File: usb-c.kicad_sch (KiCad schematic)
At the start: 37 parts, among them J2 USB-C_GCT_USB4105-GF-A, U12 FUSB303B, U13 AP22615B_TSOT26

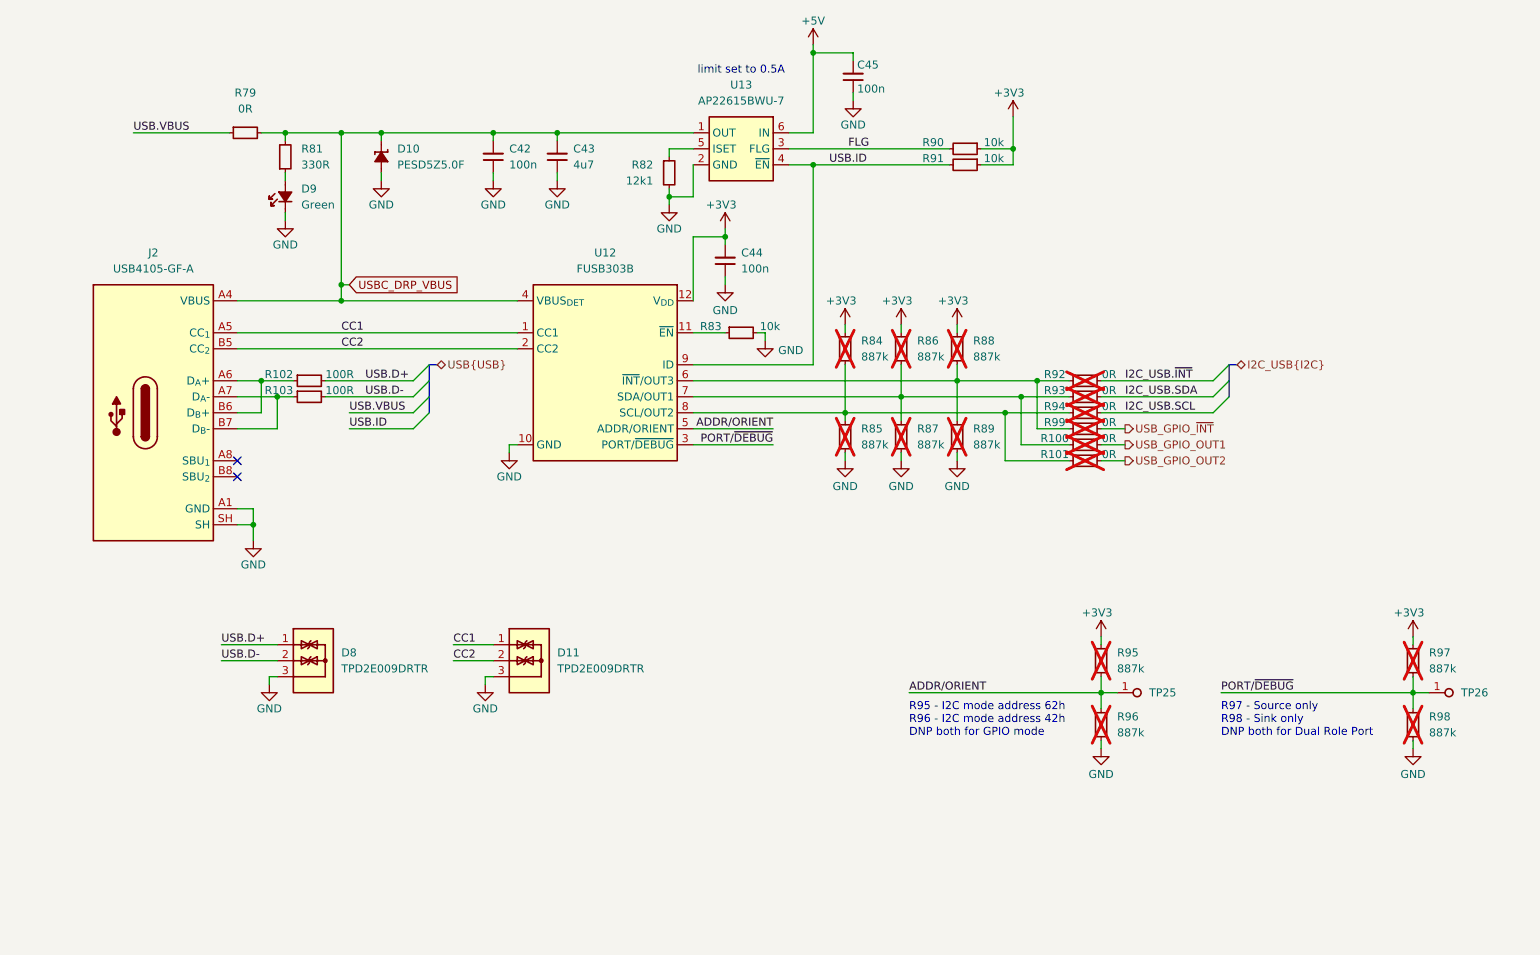
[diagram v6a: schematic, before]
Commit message: [#95036] Add testpoints
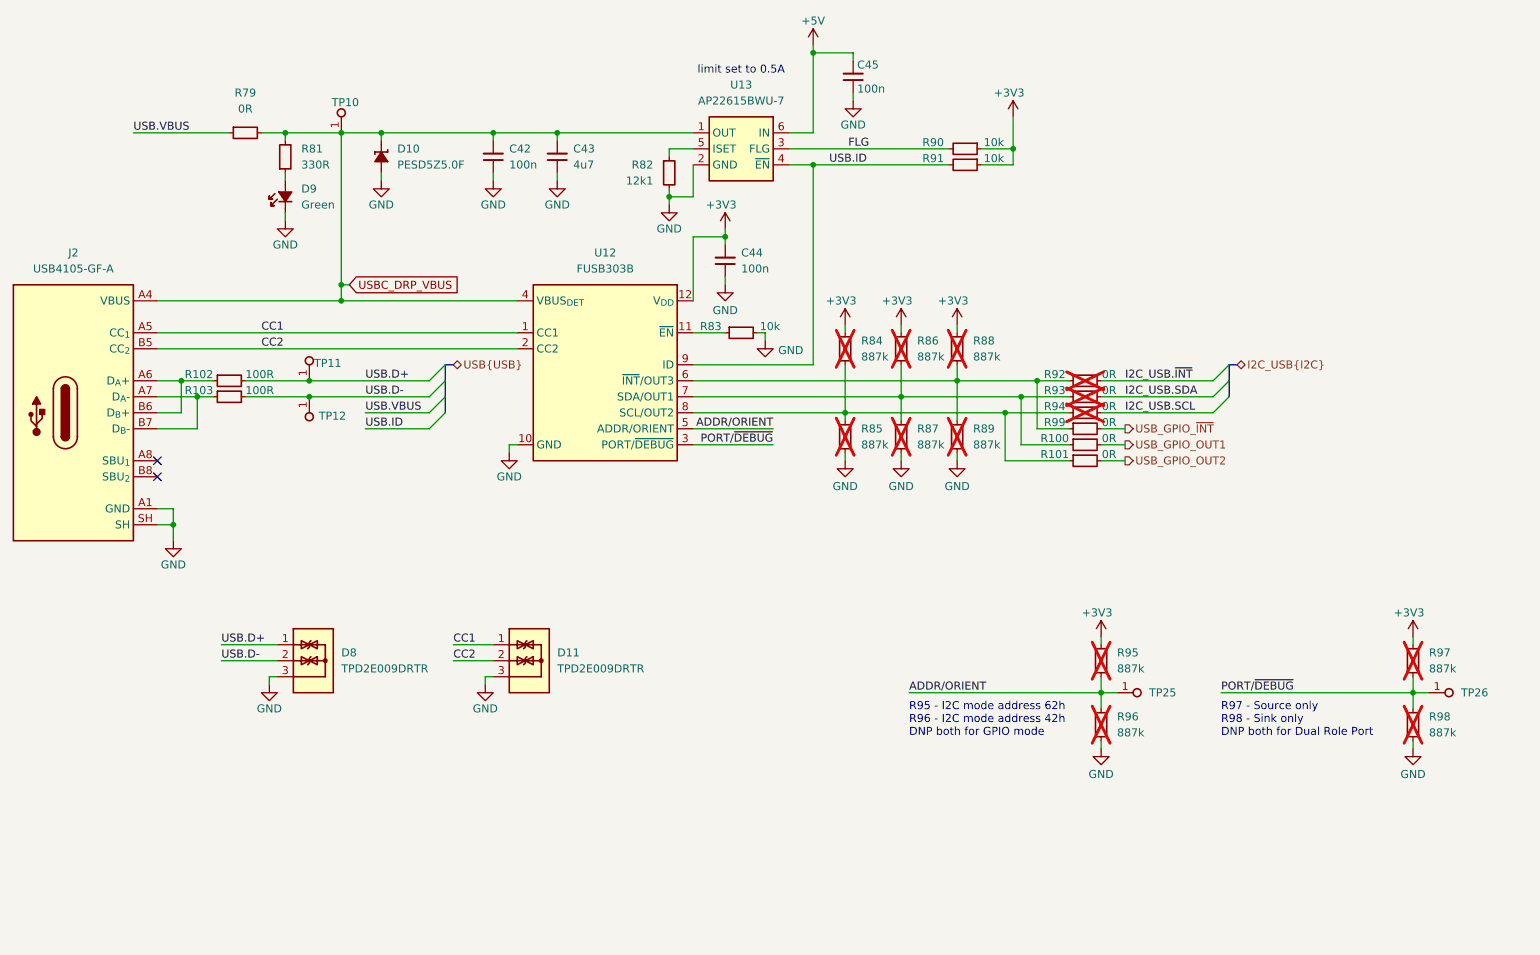
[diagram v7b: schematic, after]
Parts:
- added TP10, TP11, TP12: TP_1mm_SMD, antmicro-footprints:TP_SMD_1mm, symbol antmicroTestPoints:TP_1mm_SMD
- R100, R101, R99: now fitted
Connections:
- net USB.D+: now also TP11.1
- net USB.D-: now also TP12.1
- net USBC_DRP_VBUS: now also TP10.1
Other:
- moved on the sheet: J2, R102, R103

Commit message: [#95036] Add schematic markings
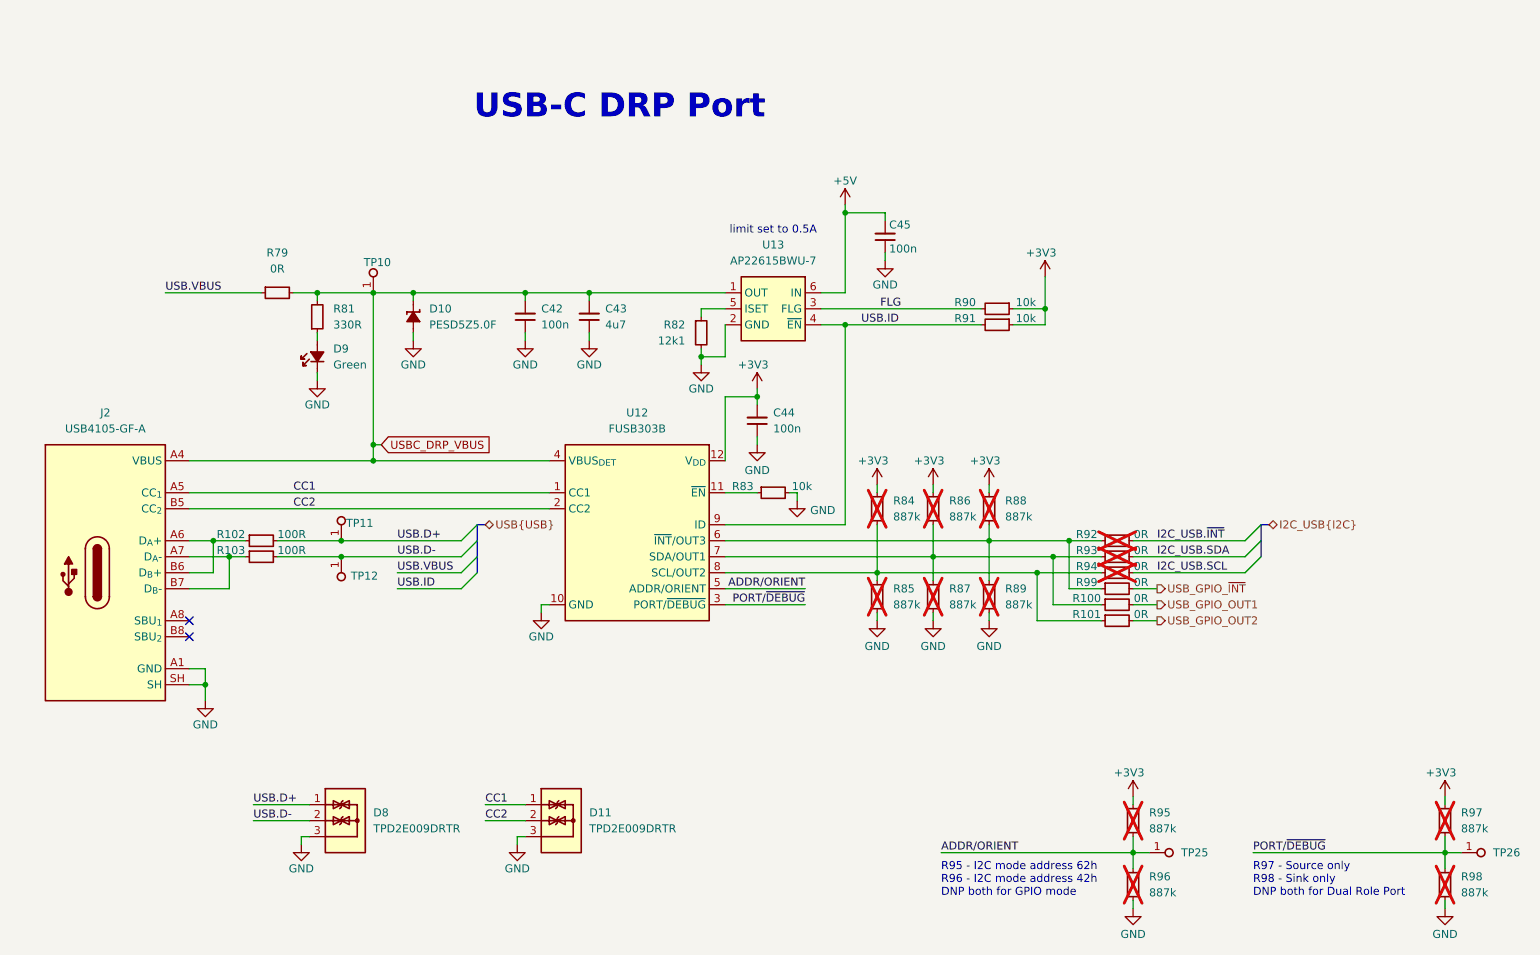
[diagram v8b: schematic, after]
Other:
- note added: "USB-C DRP Port"
- moved on the sheet: C42, C43, C44, C45, D10, D11, D8, D9, J2, R100, R101, R102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
